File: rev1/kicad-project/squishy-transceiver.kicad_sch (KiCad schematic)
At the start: 99 parts, among them Q2 Q_PMOS_DGS, Q3 Q_DUAL_PMOS_S1G1D2S2G2D1, Q4 Q_DUAL_PMOS_S1G1D2S2G2D1, U1 THVD1452DGSR, U10 THVD1452DGSR, U11 FXL4TD245BQX, U13 THVD1452DGSR, U15 THVD1452DGSR, U16 FXL4TD245BQX, U17 THVD1452DGSR, U18 THVD1452DGSR, U2 FXL4TD245BQX, U20 FXL4TD245BQX, U21 THVD1452DGSR, U22 THVD1452DGSR, U23 FXL4TD245BQX, U24 THVD1452DGSR, U25 THVD1452DGSR, U27 FXL4TD245BQX, U28 THVD1452DGSR, U29 THVD1452DGSR, U30 FXL4TD245BQX, U31 THVD1452DGSR, U32 THVD1452DGSR, U33 FXL4TD245BQX, U34 THVD1452DGSR, U4 THVD1452DGSR, U6 THVD1452DGSR, U8 FXL4TD245BQX, U9 THVD1452DGSR

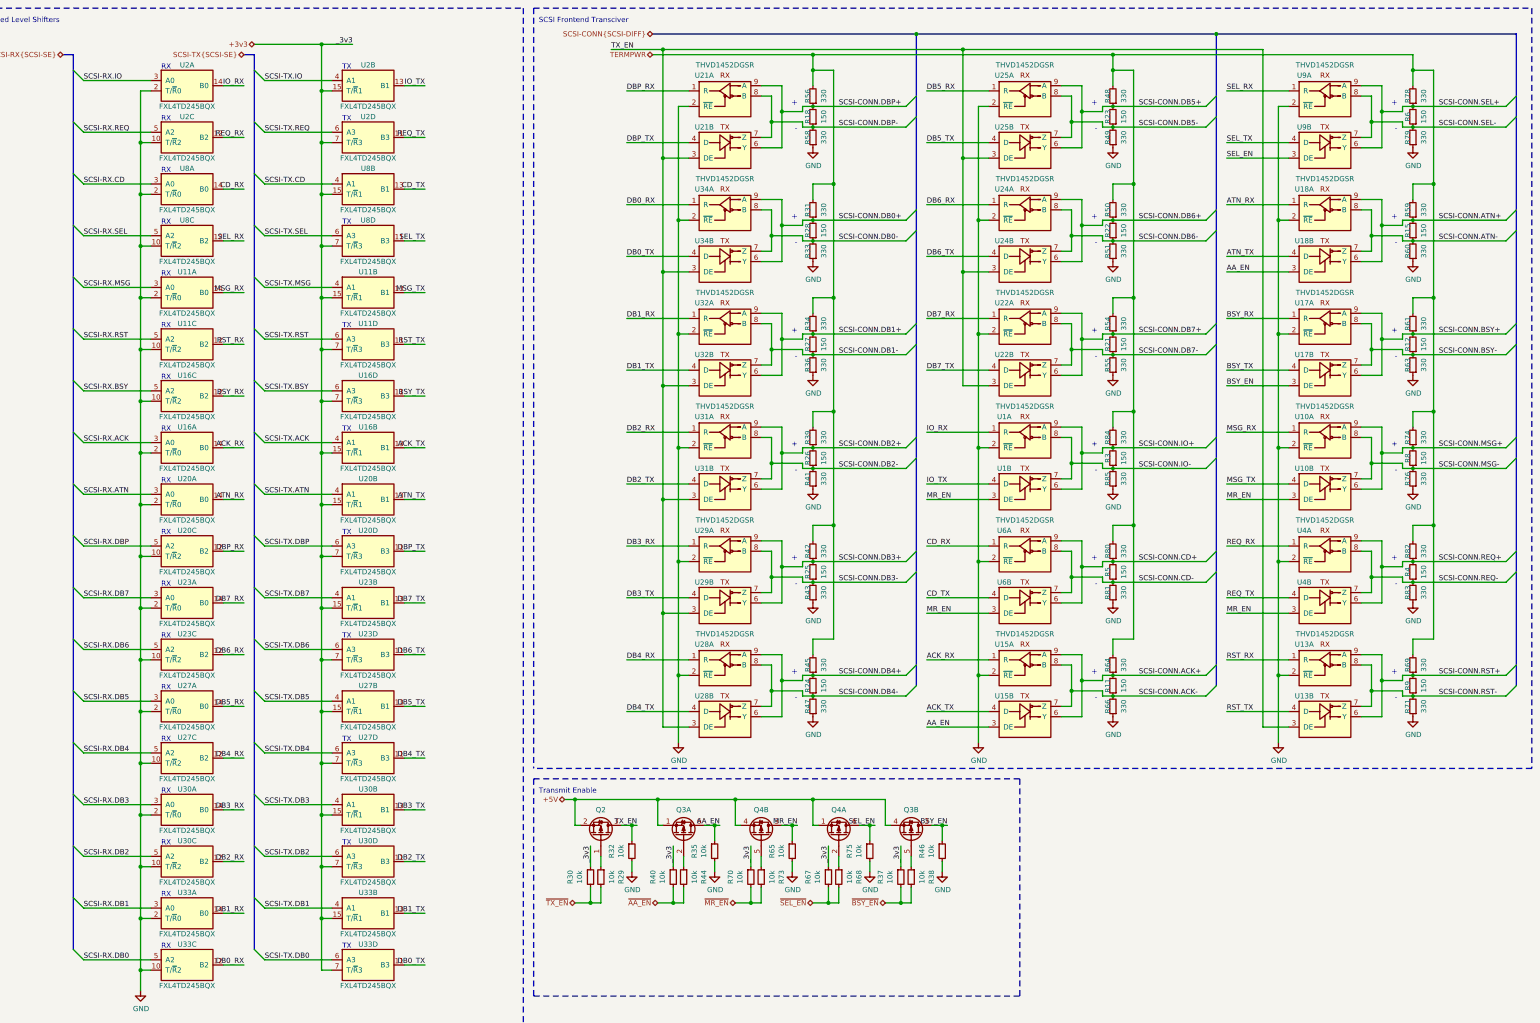
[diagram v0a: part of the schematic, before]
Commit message: hardware: added back the 1v8 regulated as we need the ULPI PHY again for USB2 compatibility, also updated the sheet metadata
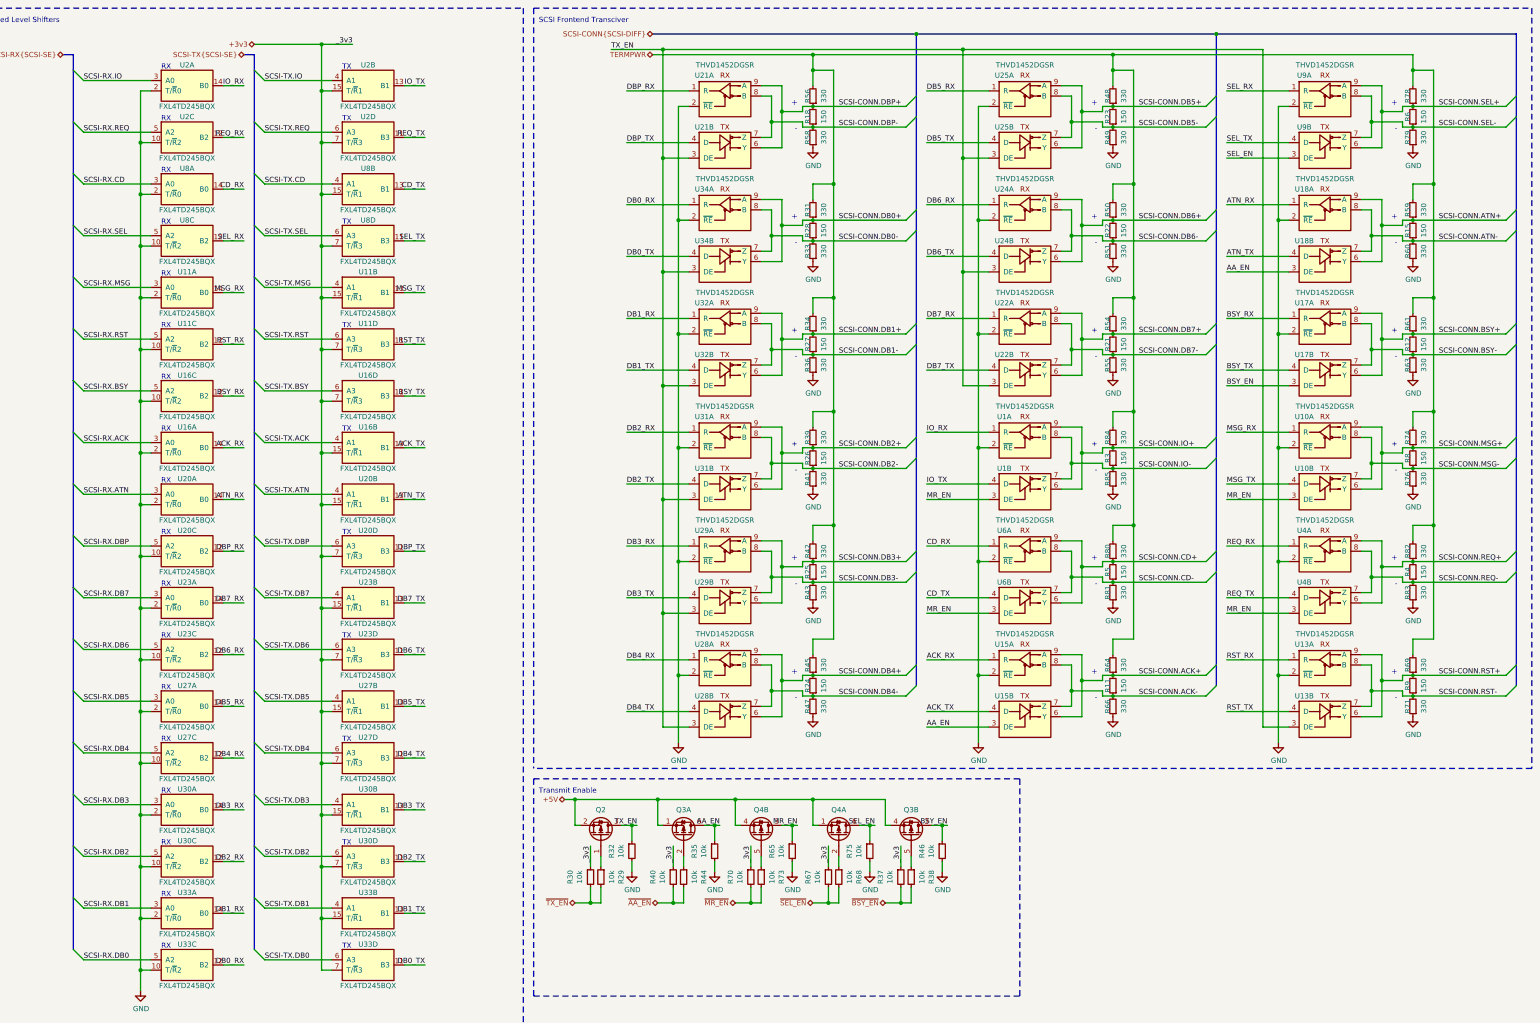
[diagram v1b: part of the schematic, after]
